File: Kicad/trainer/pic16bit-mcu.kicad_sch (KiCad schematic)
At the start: 25 parts, among them K201 MCU 1, K202 MCU 2, K203 ICSP, K204 VIN, K205 VIN, K206 VDD, K207 GND, K208 VDD, K209 GND, K210 HARWIN-254-F-1X10-VERTICAL, U201 PIC24/dsPIC33, X201 XTAL-DIL08

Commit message: Update
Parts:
- U201: footprint (none) -> tronixio:DIP-28-W762-SOCKET
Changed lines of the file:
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@@
       (effects (font (size 1.15 1.15)) (justify right))
     )
-    (property "Footprint" "" (at 144.78 101.6 0)
+    (property "Footprint" "tronixio:DIP-28-W762-SOCKET" (at 144.78 101.6 0)
       (effects (font (size 1 1)) hide)
     )

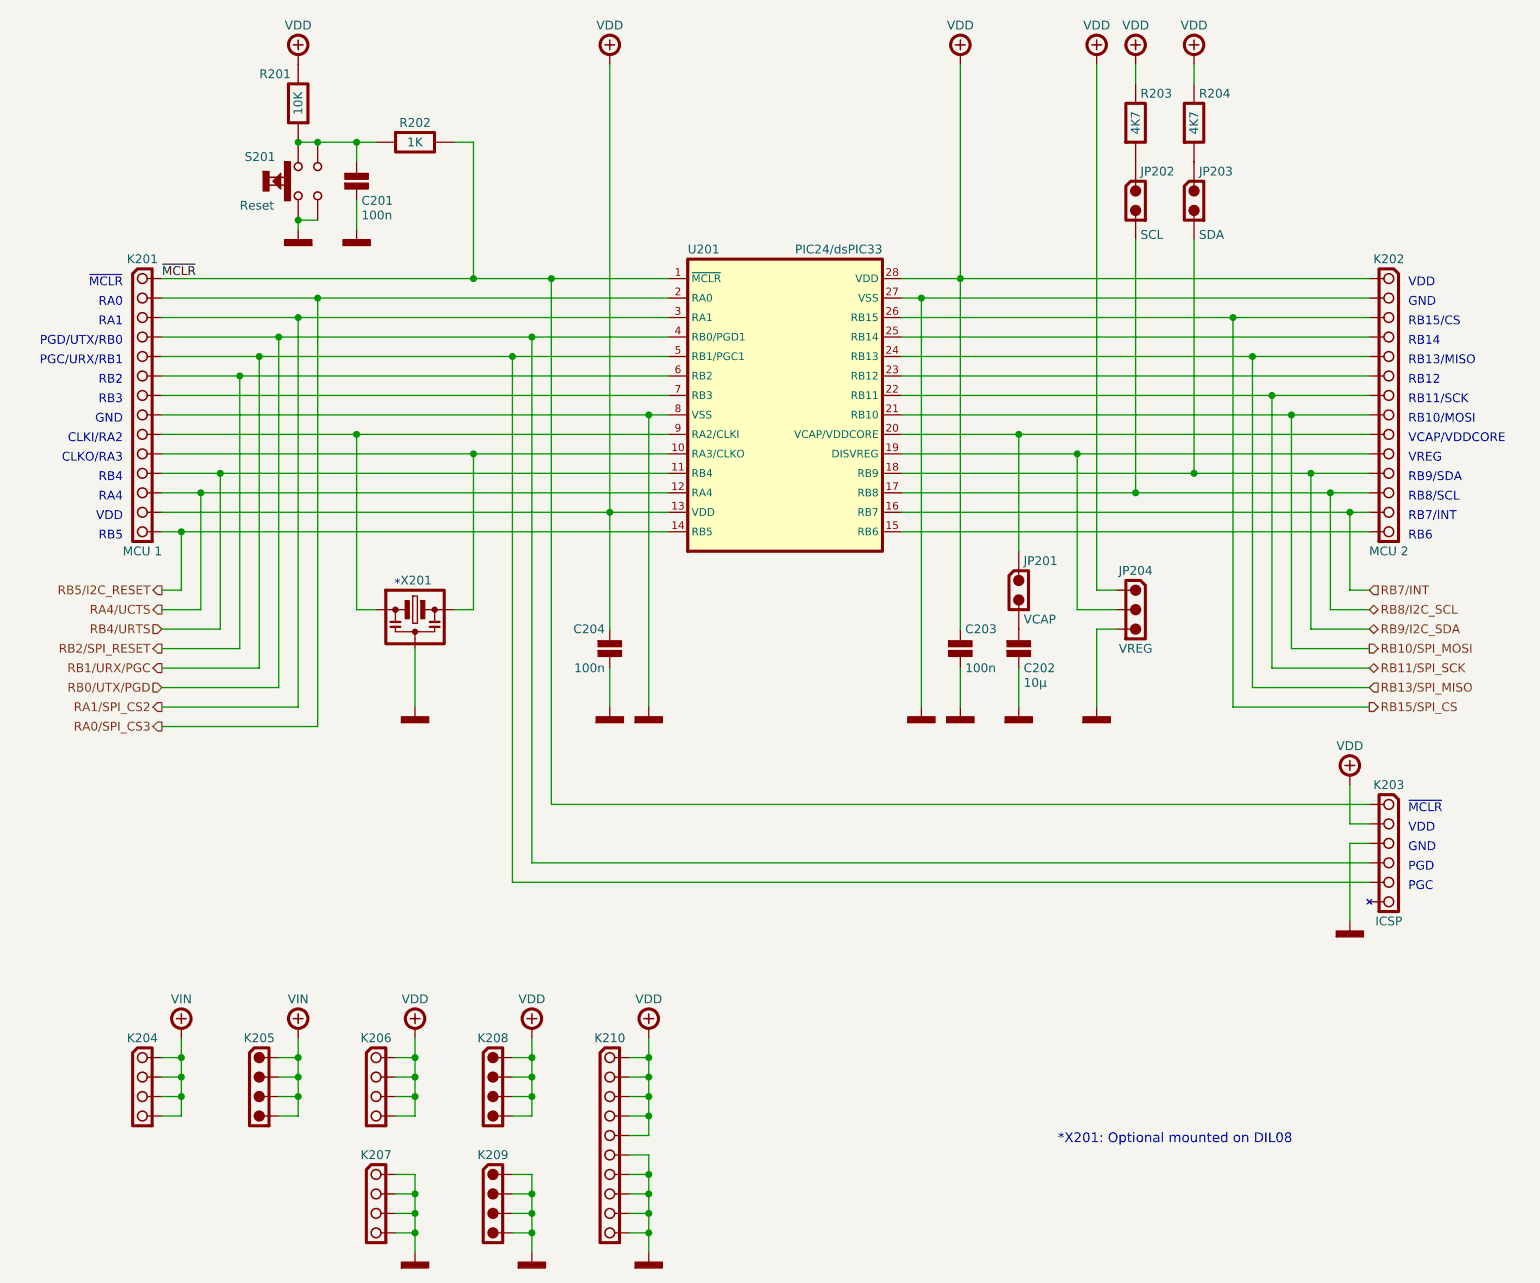
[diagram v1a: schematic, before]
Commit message: Update Trainer Kicad 8
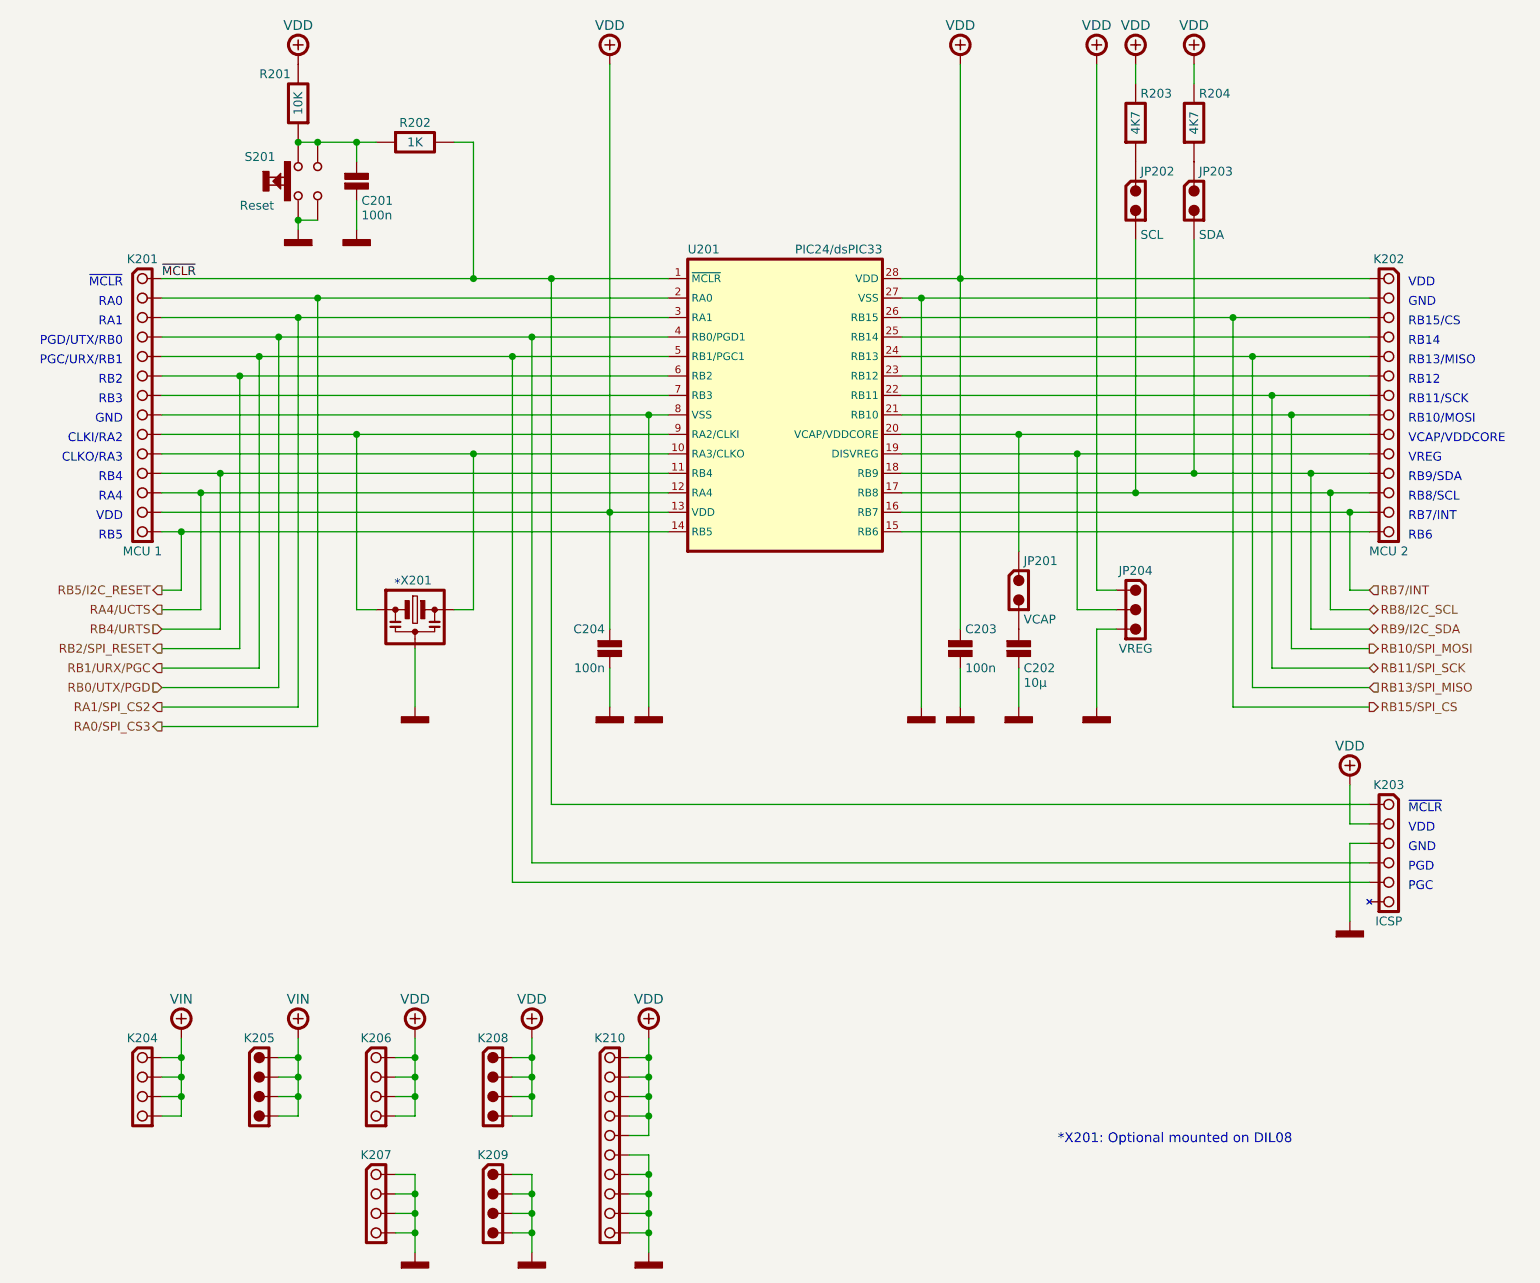
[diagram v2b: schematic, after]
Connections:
- net GND is gone; now on net POWER-GND: C201.2, C202.2, C203.2, C204.2, JP204.3, K201.8 (Pin_8), K202.2 (Pin_2), K203.4 (GND), K207.1, K207.2, K207.3, K207.4, K209.1, K209.2, K209.3, K209.4, K210.10 (Pin_10), K210.6 (Pin_6), K210.7 (Pin_7), K210.8 (Pin_8), K210.9 (Pin_9), S201.3, S201.4, U201.27 (VSS), U201.8 (VSS), X201.1
- net at K201.10 (Pin_10), U201.10 (RA3/CLKO), X201.5: now also X201.6
- net at K201.9 (Pin_9), U201.9 (RA2/CLKI), X201.3: now also X201.4
- net POWER-GND: now reaches X201.2
- net POWER-GND: now also X201.7, X201.8
- net +VDD renamed POWER-VDD
- net +VIN renamed POWER-VIN
